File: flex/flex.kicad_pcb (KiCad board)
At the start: 2 copper layers, 48.8 x 41.5 mm, 20 parts, among them J1 Conn_01x06_Female, J2 Conn_01x03_Female, SW19 SW_Push, SW5 SW_Push, SW9 SW_Push

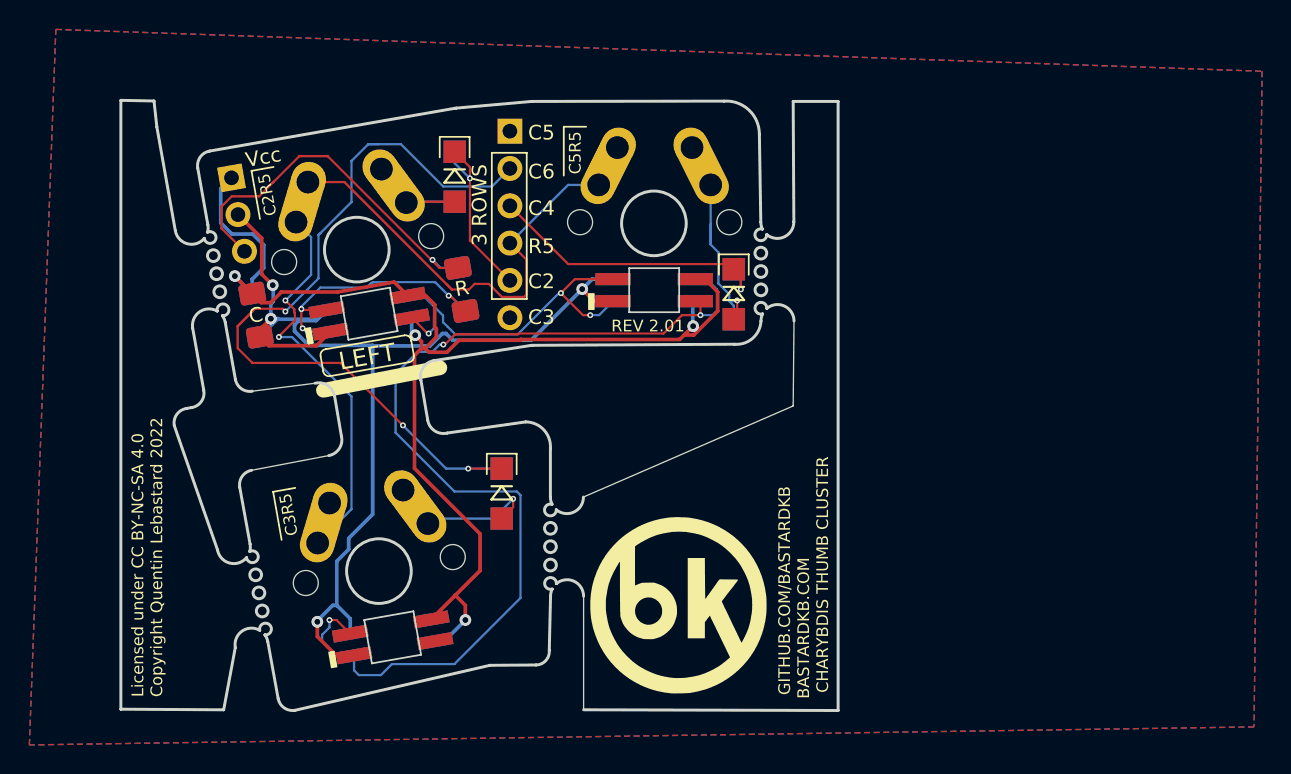
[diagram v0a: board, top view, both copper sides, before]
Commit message: pcb: remove breakout tabs and extra stuff
Signed-off-by: Anant Thazhemadam <anant.thazhemadam@gmail.com>
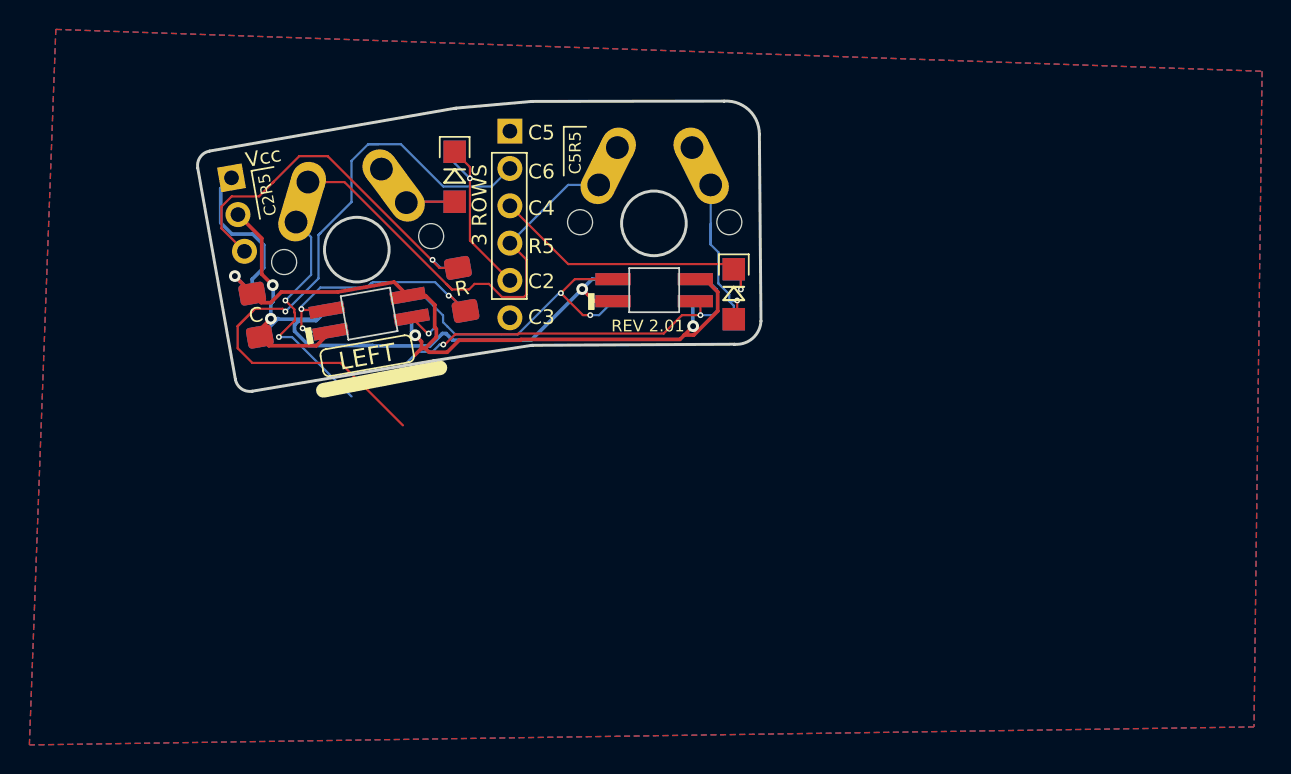
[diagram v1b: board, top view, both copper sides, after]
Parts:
- removed D2: SK6812MINI, libs2:YS-SK6812MINI-E_REVERSE
- removed D3: SK6812MINI, libs2:YS-SK6812MINI-E_REVERSE_NO_EDGECUT
- removed D9: D, custom:Diode_TH_SOD123
- removed G*** (x2): LOGO, LOGO
- removed SW9: SW_Push, custom:SW_MX_reversible
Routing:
- net Net-(D10-Pad1): track 69.9 -> 28.0 mm, vias 3 -> 2
- net Gnd: track 77.7 -> 50.8 mm, vias 4 -> 3
- net Vcc: track 87.1 -> 61.2 mm, vias 4 -> 3
- net row1: track 57.9 -> 47.0 mm
- net col6: track 56.4 -> 46.2 mm, vias 3 -> 1
- net Net-(D9-Pad2): track 8.50 -> 0.00 mm, vias 1 -> 0
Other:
- board size 48.8 x 41.5 mm -> 38.3 x 19.8 mm
- board text removed: "BASTARDKB.COM"
- board text removed: "C3R5"
- board text removed: "CHARYBDIS THUMB CLUSTER"
- board text removed: "Conn_01x02_Female"
- board text removed: "GITHUB.COM/BASTARDKB"
- board text removed: "Licensed under CC BY-NC-SA 4.0 Copyright Quentin Lebastard 2022"

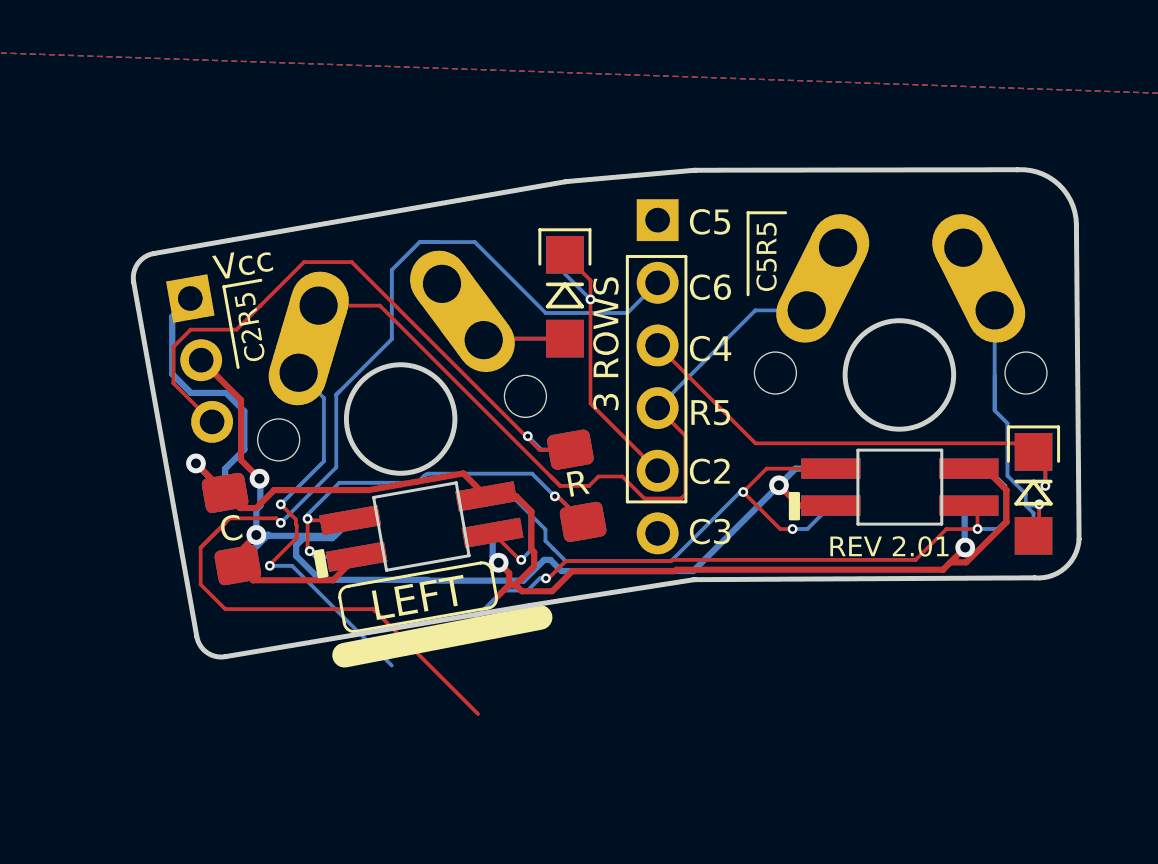
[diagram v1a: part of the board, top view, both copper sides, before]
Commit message: remove breakaway thumb
Signed-off-by: Anant Thazhemadam <anant.thazhemadam@gmail.com>
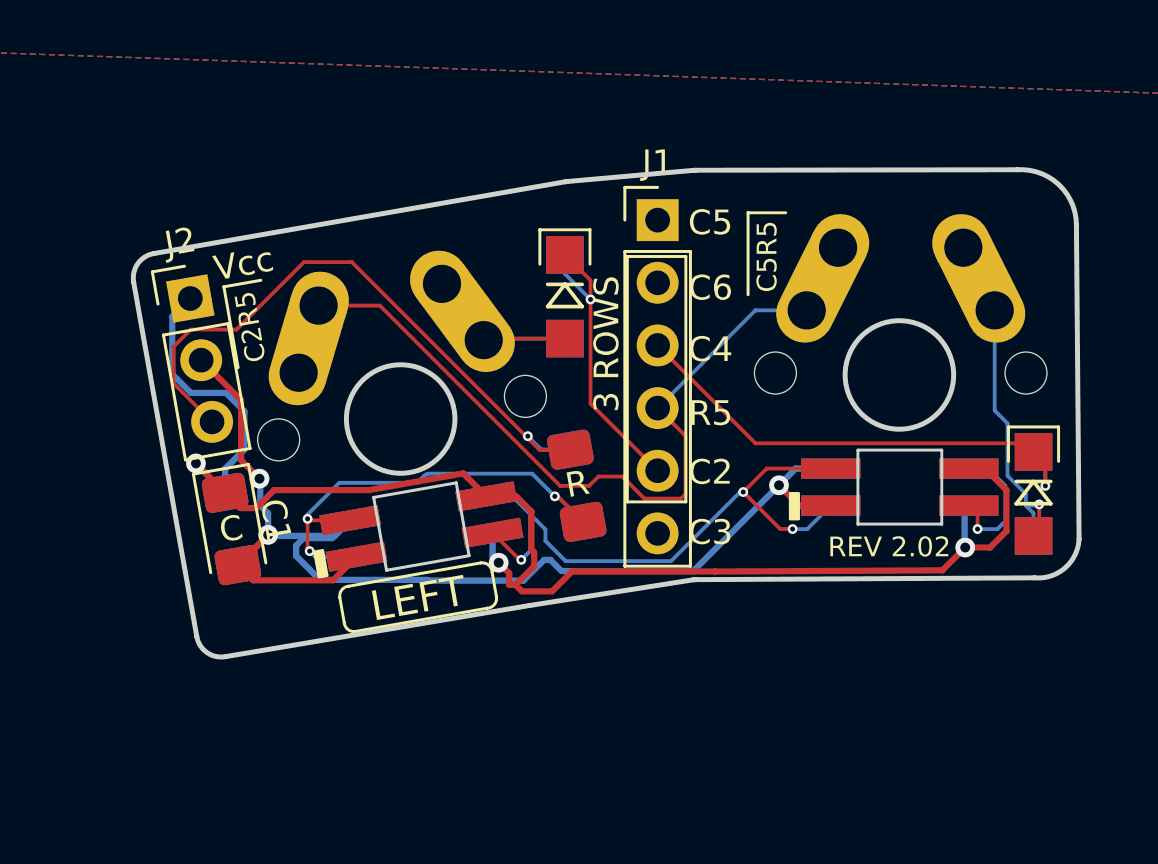
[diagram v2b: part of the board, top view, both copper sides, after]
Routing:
- net col6: track 46.2 -> 0.00 mm, vias 1 -> 0
- net Net-(D10-Pad1): track 28.0 -> 5.55 mm, vias 2 -> 1
- net row1: track 47.0 -> 30.1 mm, vias 2 -> 0
- net Net-(D19-Pad2): track 13.1 -> 11.7 mm
- net Vcc: track 61.2 -> 59.9 mm
- net Net-(D12-Pad1): track 28.0 -> 27.2 mm
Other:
- board text added: "REV 2.02"
- board text removed: "REV 2.01"
